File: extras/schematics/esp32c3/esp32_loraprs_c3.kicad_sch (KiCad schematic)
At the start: 28 parts, among them J1 Conn_Coaxial, J2 USB_C_Receptacle_USB2.0, SW1 SW_Push, U1 ESP32_C3_SuperMini, U2 E22-400M30S, U3 IP5306

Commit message: Update schematics
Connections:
- net DIO2: no longer names the net of U2.8 (DIO2)
- net DIO2: no longer U1.4 (GPIO3)
- no-connect marks 11 -> 13
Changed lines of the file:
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@@
   (no_connect (at 80.01 168.91))
   (no_connect (at 80.01 153.67))
+  (no_connect (at 203.2 72.39))
   (no_connect (at 80.01 176.53))
   (no_connect (at 80.01 156.21))
@@
   (no_connect (at 80.01 163.83))
   (no_connect (at 160.02 40.64))
+  (no_connect (at 135.89 43.18))
   (no_connect (at 135.89 48.26))
   (no_connect (at 135.89 38.1))
@@
     )
   )
-  (global_label "DIO2" (shape input) (at 203.2 72.39 180) (fields_autoplaced)
-    (effects (font (size 1.27 1.27)) (justify right))
-    (property "Intersheet References" "${INTERSHEET_REFS}" (id 0) (at 196.3721 72.3106 0)
-      (effects (font (size 1.27 1.27)) (justify right) hide)
-    )
-  )
   (global_label "B+" (shape input) (at 111.76 93.98 90) (fields_autoplaced)
     (effects (font (size 1.27 1.27)) (justify left))
@@
       (effects (font (size 1.27 1.27)) (justify right) hide)
     )
-  )
-  (global_label "DIO2" (shape input) (at 135.89 43.18 180) (fields_autoplaced)
-    (effects (font (size 1.27 1.27)) (justify right))
-    (property "Intersheet References" "${INTERSHEET_REFS}" (id 0) (at 129.0621 43.1006 0)
-      (effects (font (size 1.27 1.27)) (justify right) hide)
-    )

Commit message: Update schematics
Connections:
- net BUSY: now also U1.14 (GPIO10); no longer U1.13 (GPIO9)
- net DIO1: now also U1.4 (GPIO3); no longer U1.3 (GPIO2)
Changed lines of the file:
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@@
   )
   (no_connect (at 80.01 168.91))
+  (no_connect (at 135.89 40.64))
   (no_connect (at 80.01 153.67))
   (no_connect (at 203.2 72.39))
@@
   (no_connect (at 80.01 179.07))
   (no_connect (at 80.01 161.29))
+  (no_connect (at 160.02 43.18))
   (no_connect (at 80.01 166.37))
   (no_connect (at 80.01 163.83))
-  (no_connect (at 160.02 40.64))
-  (no_connect (at 135.89 43.18))
   (no_connect (at 135.89 48.26))
   (no_connect (at 135.89 38.1))
@@
     )
   )
-  (global_label "BUSY" (shape input) (at 160.02 43.18 0) (fields_autoplaced)
-    (effects (font (size 1.27 1.27)) (justify left))
-    (property "Intersheet References" "${INTERSHEET_REFS}" (id 0) (at 167.3317 43.1006 0)
+  (global_label "BUSY" (shape input) (at 160.02 40.64 0) (fields_autoplaced)
+    (effects (font (size 1.27 1.27)) (justify left))
+    (property "Intersheet References" "${INTERSHEET_REFS}" (id 0) (at 167.3317 40.5606 0)
       (effects (font (size 1.27 1.27)) (justify left) hide)
     )
@@
     )
   )
-  (global_label "DIO1" (shape input) (at 135.89 40.64 180) (fields_autoplaced)
+  (global_label "DIO1" (shape input) (at 135.89 43.18 180) (fields_autoplaced)
     (effects (font (size 1.27 1.27)) (justify right))
-    (property "Intersheet References" "${INTERSHEET_REFS}" (id 0) (at 129.0621 40.7194 0)
+    (property "Intersheet References" "${INTERSHEET_REFS}" (id 0) (at 129.0621 43.2594 0)
       (effects (font (size 1.27 1.27)) (justify right) hide)
     )

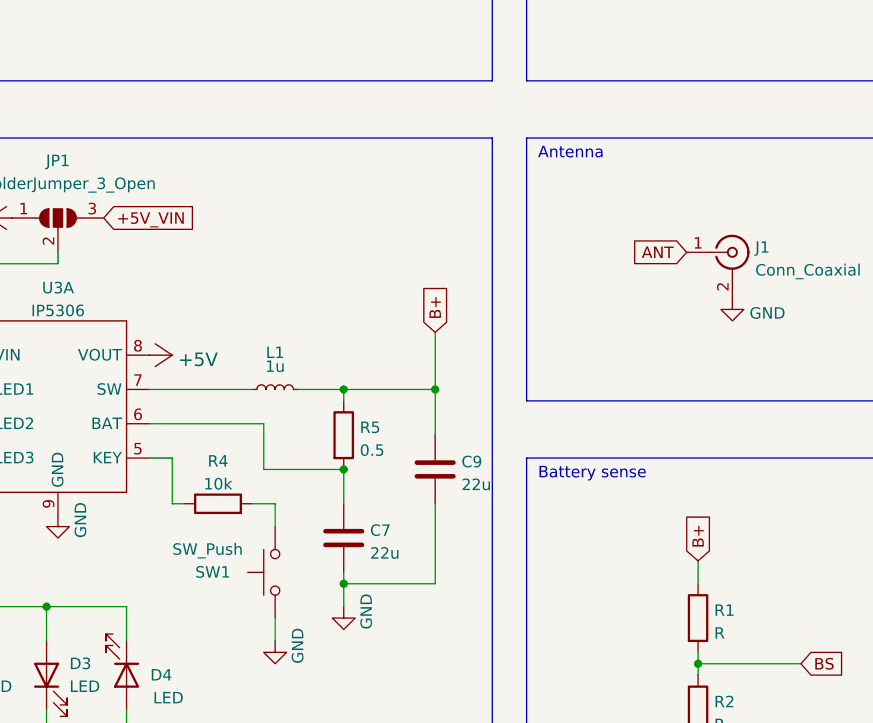
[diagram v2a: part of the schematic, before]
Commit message: Added DIP switch for battery
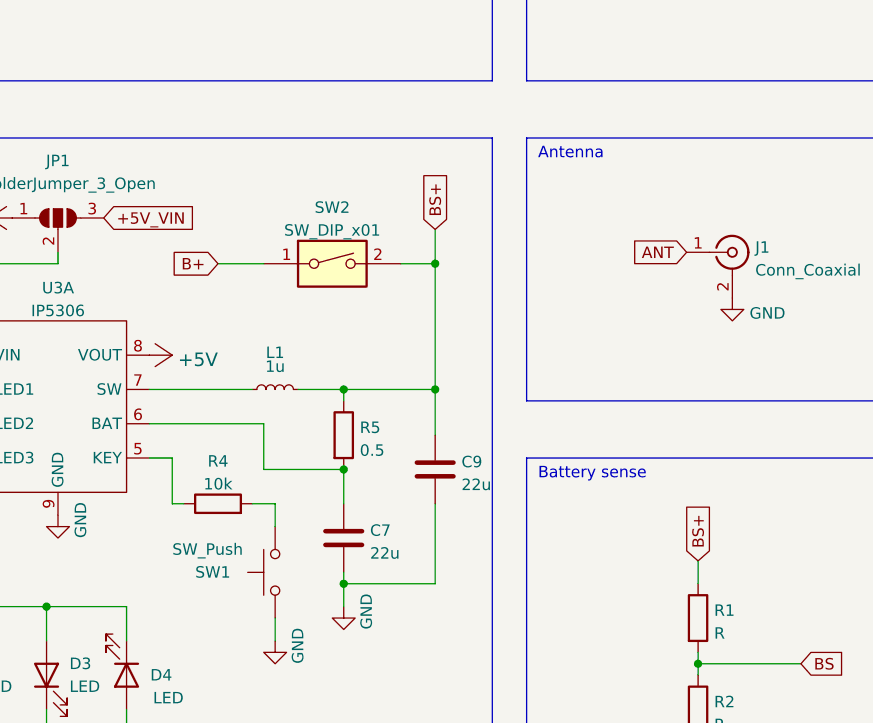
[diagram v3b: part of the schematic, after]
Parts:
- added SW2: SW_DIP_x01, Button_Switch_SMD:SW_SPST_REED_CT05-XXXX-J1, symbol Switch:SW_DIP_x01
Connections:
- net B+: now also SW2.1; no longer C9.1, L1.2, R1.1, R5.1
- new net BS+: C9.1, L1.2, R1.1, R5.1, SW2.2
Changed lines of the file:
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@@
   (junction (at 100.33 50.8) (diameter 0) (color 0 0 0 0)
   )
+  (junction (at 111.76 86.36) (diameter 0) (color 0 0 0 0)
+  )
   (junction (at 82.55 38.1) (diameter 0) (color 0 0 0 0)
   )
@@
   (junction (at 71.12 38.1) (diameter 0) (color 0 0 0 0)
   )
+  (junction (at 101.6 121.92) (diameter 0) (color 0 0 0 0)
+  )
+  (junction (at 68.58 139.7) (diameter 0) (color 0 0 0 0)
+  )
+  (junction (at 91.44 50.8) (diameter 0) (color 0 0 0 0)
+  )
+  (junction (at 101.6 109.22) (diameter 0) (color 0 0 0 0)
+  )
+  (junction (at 199.39 128.27) (diameter 0) (color 0 0 0 0)
+  )
+  (junction (at 62.23 38.1) (diameter 0) (color 0 0 0 0)
+  )
+  (junction (at 71.12 50.8) (diameter 0) (color 0 0 0 0)
+  )
+  (junction (at 99.06 148.59) (diameter 0) (color 0 0 0 0)
+  )
   (junction (at 111.76 100.33) (diameter 0) (color 0 0 0 0)
-  )
-  (junction (at 101.6 121.92) (diameter 0) (color 0 0 0 0)
-  )
-  (junction (at 68.58 139.7) (diameter 0) (color 0 0 0 0)
-  )
-  (junction (at 91.44 50.8) (diameter 0) (color 0 0 0 0)
-  )
-  (junction (at 101.6 109.22) (diameter 0) (color 0 0 0 0)
-  )
-  (junction (at 199.39 128.27) (diameter 0) (color 0 0 0 0)
-  )
-  (junction (at 62.23 38.1) (diameter 0) (color 0 0 0 0)
-  )
-  (junction (at 71.12 50.8) (diameter 0) (color 0 0 0 0)
-  )
-  (junction (at 99.06 148.59) (diameter 0) (color 0 0 0 0)
   )
   (junction (at 58.42 139.7) (diameter 0) (color 0 0 0 0)
@@
     (stroke (width 0) (type default) (color 0 0 0 0))
   )
+  (wire (pts (xy 87.63 86.36) (xy 92.71 86.36))
+    (stroke (width 0) (type default) (color 0 0 0 0))
+  )
   (wire (pts (xy 92.71 109.22) (xy 92.71 104.14))
     (stroke (width 0) (type default) (color 0 0 0 0))
@@
     (stroke (width 0) (type default) (color 0 0 0 0))
   )
+  (wire (pts (xy 107.95 86.36) (xy 111.76 86.36))
+    (stroke (width 0) (type default) (color 0 0 0 0))
+  )
   (wire (pts (xy 140.97 139.7) (xy 140.97 143.51))
     (stroke (width 0) (type default) (color 0 0 0 0))
@@
     (stroke (width 0) (type default) (color 0 0 0 0))
   )
+  (wire (pts (xy 111.76 82.55) (xy 111.76 86.36))
+    (stroke (width 0) (type default) (color 0 0 0 0))
+  )
   (polyline (pts (xy 121.92 107.95) (xy 168.91 107.95))
     (stroke (width 0) (type default) (color 0 0 0 0))
@@
     (stroke (width 0) (type default) (color 0 0 0 0))
   )
-  (wire (pts (xy 111.76 93.98) (xy 111.76 100.33))
-    (stroke (width 0) (type default) (color 0 0 0 0))
-  )
   (wire (pts (xy 101.6 120.65) (xy 101.6 121.92))
     (stroke (width 0) (type default) (color 0 0 0 0))
@@
   )
   (wire (pts (xy 95.25 172.72) (xy 95.25 175.26))
+    (stroke (width 0) (type default) (color 0 0 0 0))
+  )
+  (wire (pts (xy 111.76 86.36) (xy 111.76 100.33))
     (stroke (width 0) (type default) (color 0 0 0 0))
   )
@@
     (effects (font (size 1.27 1.27)) (justify left bottom))
   )
+  (global_label "BS+" (shape input) (at 111.76 82.55 90) (fields_autoplaced)
+    (effects (font (size 1.27 1.27)) (justify left))
+    (property "Intersheet References" "${INTERSHEET_REFS}" (id 0) (at 111.8394 76.085 90)
+      (effects (font (size 1.27 1.27)) (justify left) hide)
+    )
+  )
   (global_label "NSS" (shape input) (at 254 52.07 0) (fields_autoplaced)
     (effects (font (size 1.27 1.27)) (justify left))
@@
     (effects (font (size 1.27 1.27)) (justify left))
     (property "Intersheet References" "${INTERSHEET_REFS}" (id 0) (at 261.0093 67.2306 0)
-      (effects (font (size 1.27 1.27)) (justify left) hide)
-    )
-  )
-  (global_label "B+" (shape input) (at 140.97 119.38 90) (fields_autoplaced)
-    (effects (font (size 1.27 1.27)) (justify left))
-    (property "Intersheet References" "${INTERSHEET_REFS}" (id 0) (at 141.0494 114.1245 90)
       (effects (font (size 1.27 1.27)) (justify left) hide)
     )
@@
     )
   )
-  (global_label "B+" (shape input) (at 111.76 93.98 90) (fields_autoplaced)
-    (effects (font (size 1.27 1.27)) (justify left))
-    (property "Intersheet References" "${INTERSHEET_REFS}" (id 0) (at 111.8394 88.7245 90)
-      (effects (font (size 1.27 1.27)) (justify left) hide)
+  (global_label "B+" (shape input) (at 87.63 86.36 180) (fields_autoplaced)
+    (effects (font (size 1.27 1.27)) (justify right))
+    (property "Intersheet References" "${INTERSHEET_REFS}" (id 0) (at 82.3745 86.2806 0)
+      (effects (font (size 1.27 1.27)) (justify right) hide)
     )
   )
@@
     (property "Intersheet References" "${INTERSHEET_REFS}" (id 0) (at 130.9974 35.4806 0)
       (effects (font (size 1.27 1.27)) (justify right) hide)
+    )
+  )
+  (global_label "BS+" (shape input) (at 140.97 119.38 90) (fields_autoplaced)
+    (effects (font (size 1.27 1.27)) (justify left))
+    (property "Intersheet References" "${INTERSHEET_REFS}" (id 0) (at 141.0494 112.915 90)
+      (effects (font (size 1.27 1.27)) (justify left) hide)
     )
   )
@@
     )
     (property "Datasheet" " ~" (id 3) (at 144.78 85.09 0)
+      (effects (font (size 1.27 1.27)) hide)
+    )
+    (pin "1")
+    (pin "2")
+  )
+  (symbol (lib_id "Switch:SW_DIP_x01") (at 100.33 86.36 0) (unit 1)
+    (in_bom yes) (on_board yes) (fields_autoplaced)
+    (property "Reference" "SW2" (id 0) (at 100.33 80.1202 0))
+    (property "Value" "SW_DIP_x01" (id 1) (at 100.33 82.6571 0))
+    (property "Footprint" "Button_Switch_SMD:SW_SPST_REED_CT05-XXXX-J1" (id 2) (at 100.33 86.36 0)
+      (effects (font (size 1.27 1.27)) hide)
+    )
+    (property "Datasheet" "~" (id 3) (at 100.33 86.36 0)
       (effects (font (size 1.27 1.27)) hide)
     )
@@
       (reference "SW1") (unit 1) (value "SW_Push") (footprint "Button_Switch_SMD:Panasonic_EVQPUJ_EVQPUA")
     )
+    (path "/b34b9d3f-826f-45a3-9e7e-523e468bd023"
+      (reference "SW2") (unit 1) (value "SW_DIP_x01") (footprint "Button_Switch_SMD:SW_SPST_REED_CT05-XXXX-J1")
+    )
     (path "/9b3e5cb2-e742-4a8f-b4f9-e8f7bc6b39bb"
